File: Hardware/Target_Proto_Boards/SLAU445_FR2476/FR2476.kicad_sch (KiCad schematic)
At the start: 44 parts, among them J1 USB_B_Micro, J10 PORT6, J11 PORT3, J12 JTAG/SBW, J13 VSEL, J14 VCC, J15 GND, J16 +5V, J17 GND, J4 LED_P4.1, J5 DEBUG, J6 PORT4, J7 PORT1, J8 PORT5, J9 PORT2, SW1 TL-2203, SW2 RESET, U1 MSP430FR2476TPTR, U2 AMS1117-3.3, Y1 32768 12pF

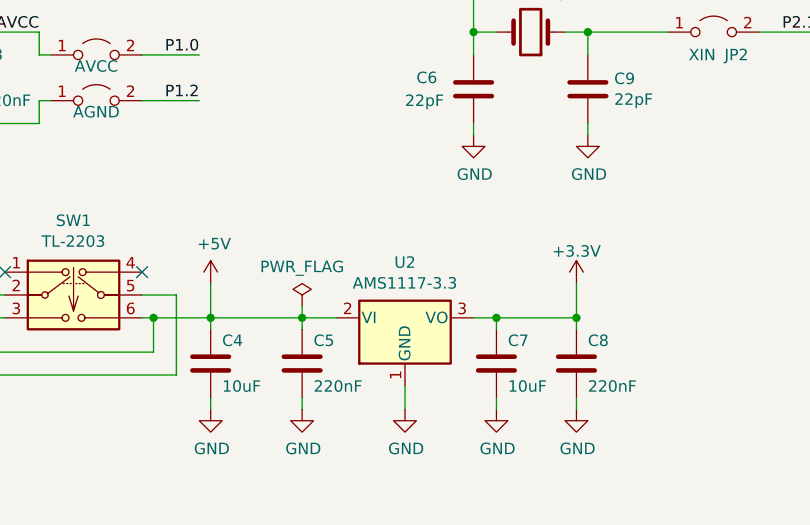
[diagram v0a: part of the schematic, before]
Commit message: Fixed regulator part#
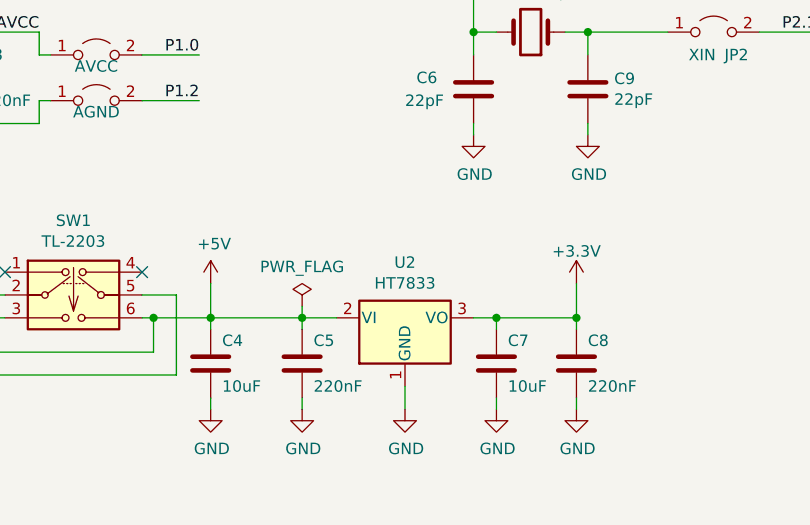
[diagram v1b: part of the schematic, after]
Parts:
- U2: value AMS1117-3.3 -> HT7833
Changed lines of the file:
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@@
     (in_bom yes) (on_board yes)
     (property "Reference" "U2" (id 0) (at 87.63 162.7632 0))
-    (property "Value" "AMS1117-3.3" (id 1) (at 87.63 165.0746 0))
+    (property "Value" "HT7833" (id 1) (at 87.63 165.0746 0))
     (property "Footprint" "Package_TO_SOT_SMD:SOT-89-3_Handsoldering" (id 2) (at 87.63 163.83 0)
       (effects (font (size 1.27 1.27)) hide)
@@
     )
     (path "/00000000-0000-0000-0000-0000610e48b7"
-      (reference "U2") (unit 1) (value "AMS1117-3.3") (footprint "Package_TO_SOT_SMD:SOT-89-3_Handsoldering")
+      (reference "U2") (unit 1) (value "HT7833") (footprint "Package_TO_SOT_SMD:SOT-89-3_Handsoldering")
     )
     (path "/00000000-0000-0000-0000-00006144b8ff"
